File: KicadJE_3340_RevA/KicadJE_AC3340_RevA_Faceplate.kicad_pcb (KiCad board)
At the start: 2 copper layers, 40 x 128 mm, 20 parts

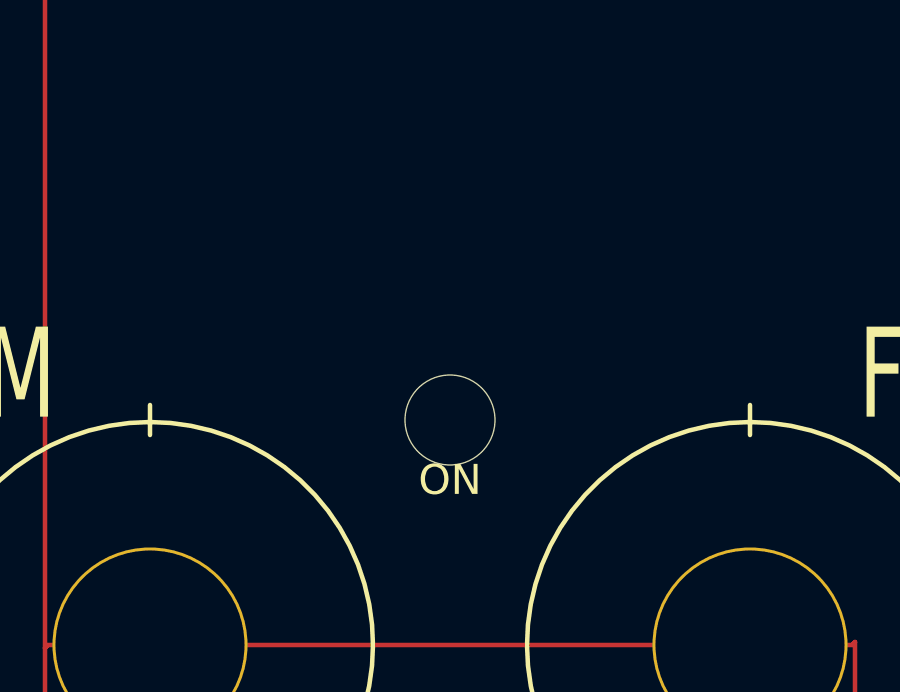
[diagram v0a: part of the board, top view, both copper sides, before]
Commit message: LED PWR moved
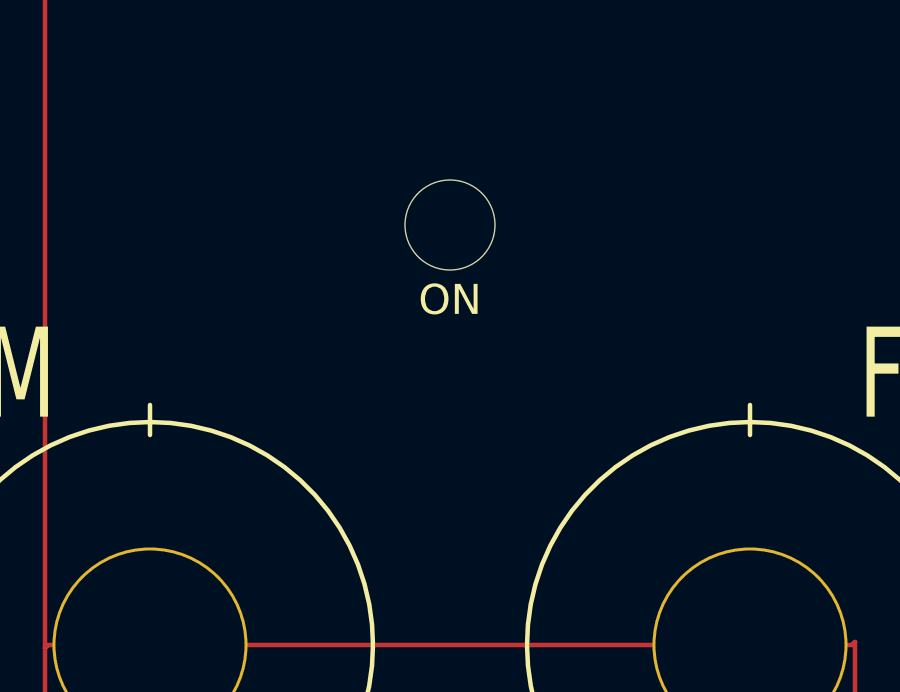
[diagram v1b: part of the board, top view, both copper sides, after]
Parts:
- moved TP114 6.50 mm to (-30.0, 51.0)
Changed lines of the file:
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@@
   )
   (module AJ:LED_Hole_3mm (layer F.Cu)
-    (at -30 57.5)
+    (at -30 51)
     (descr "Mounting Hole 2.5mm, no annular")
     (tags "mounting hole 2.5mm no annular")
@@
       (effects (font (size 1 1) (thickness 0.15)))
     )
-    (fp_text value ON (at 0 2) (layer F.SilkS)
+    (fp_text value ON (at 0 2.5) (layer F.SilkS)
       (effects (font (size 1 1) (thickness 0.15)))
     )

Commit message: JLC order number
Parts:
- removed the REF** at (-40.0, 125.0)
- removed the REF** at (-40.0, 105.0)
- removed the REF** at (-40.0, 115.0)
- removed the REF** at (-20.0, 115.0)
- removed the REF** at (-20.0, 125.0)
- removed the REF** at (-20.0, 135.0)
- removed the REF** at (-40.0, 135.0)
- removed the REF** at (-40.0, 145.0)
- removed the REF** at (-20.0, 145.0)
- removed the REF** at (-16.5, 39.0)
- removed the REF** at (-43.5, 39.0)
- removed the REF** at (-16.5, 161.0)
- removed the REF** at (-20.0, 65.0)
- removed the REF** at (-40.0, 65.0)
- removed the REF** at (-40.0, 85.0)
- removed the REF** at (-40.0, 95.0)
- added REF**: 6,3mm inner, AJ:Jack_6m3, F.Cu at (60.0, 125.0)
- added REF**: 6,3mm inner, AJ:Jack_6m3, F.Cu at (60.0, 105.0)
- added REF**: 6,3mm inner, AJ:Jack_6m3, F.Cu at (60.0, 115.0)
- added REF**: 6,3mm inner, AJ:Jack_6m3, F.Cu at (80.0, 115.0)
- added REF**: 6,3mm inner, AJ:Jack_6m3, F.Cu at (80.0, 125.0)
- added REF**: 6,3mm inner, AJ:Jack_6m3, F.Cu at (80.0, 135.0)
- added REF**: 6,3mm inner, AJ:Jack_6m3, F.Cu at (60.0, 135.0)
- added REF**: 6,3mm inner, AJ:Jack_6m3, F.Cu at (60.0, 145.0)
- added REF**: 6,3mm inner, AJ:Jack_6m3, F.Cu at (80.0, 145.0)
- added REF**: MountingHole_Eurorack2, AJ:MountingHole_Eurorack2, F.Cu at (83.5, 39.0)
- added REF**: MountingHole_Eurorack2, AJ:MountingHole_Eurorack2, F.Cu at (56.5, 39.0)
- added REF**: MountingHole_Eurorack2, AJ:MountingHole_Eurorack2, F.Cu at (83.5, 161.0)
- added REF**: 6,3mm inner pot, AJ:Pot_6m3_scale1, F.Cu at (80.0, 65.0)
- added REF**: 6,3mm inner pot, AJ:Pot_6m3_scale1, F.Cu at (60.0, 65.0)
- added REF**: 6,3mm inner, AJ:Jack_6m3, F.Cu at (60.0, 85.0)
- added REF**: 6,3mm inner, AJ:Jack_6m3, F.Cu at (60.0, 95.0)
- moved G*** 100.0 mm to (70.0, 160.5)
- moved REF** 100.0 mm to (56.5, 161.0)
- moved REF** 100.0 mm to (80.0, 100.0)
- moved TP114 100.0 mm to (70.0, 51.0)
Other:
- board text added: "JLCJLCJLCJLC"
